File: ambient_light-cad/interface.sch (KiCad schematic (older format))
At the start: 0 parts

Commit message: [Updated] move interface page and global label
interface 페이지에 들어가는 부품 이동 및 페이지 간 라벨링을 위해 Global label로 변경
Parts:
- added C?: 4.7μF, symbol Device:CP1_Small
- added C? (x4): 220μF, symbol Device:CP1_Small
- added J?: USB_C_Receptacle_USB2.0, symbol Connector:USB_C_Receptacle_USB2.0
- added J?: LED_Strip_conn_1, symbol Connector:Conn_01x03_Female
- added J?: LED_Strip_conn_2, symbol Connector:Conn_01x03_Female
- added J?: ICSP, symbol Connector_Generic:Conn_02x03_Odd_Even
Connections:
- net labels added: +5V, D+, D-, D6, D7, GND, MISO, MOSI, Reset, SCK, VBUS, VCC
- wire segments 0 -> 42
- no-connect marks 0 -> 4

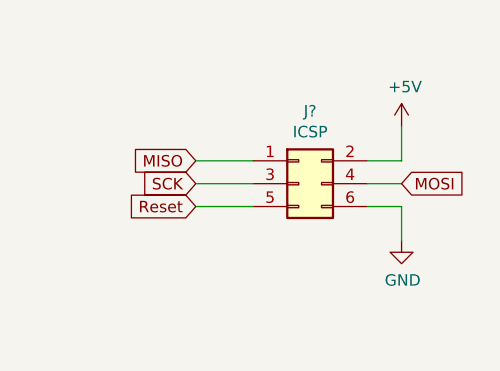
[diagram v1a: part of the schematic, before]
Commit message: [Modified] +5V to VCC /interface
전에 USBVCC와 레귤레이터 5V 분리를 위해서 섞인 VCC와 +5V를 단일화 시킴
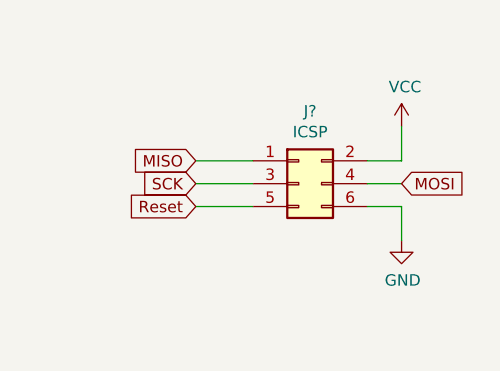
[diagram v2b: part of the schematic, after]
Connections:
- net labels removed: +5V
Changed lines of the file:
@@
 	7750 1750 7750 1900
-$Comp
-L power:+5V #PWR?
-U 1 1 5FDA9512
-P 7750 1400
-AR Path="/5FDA9512" Ref="#PWR?"  Part="1"
-AR Path="/5FD145BE/5FDA9512" Ref="#PWR?"  Part="1"
-AR Path="/5FD145BE/5FD7B477/5FDA9512" Ref="#PWR?"  Part="1"
-F 0 "#PWR?" H 7750 1250 50  0001 C CNN
-F 1 "+5V" H 7765 1573 50  0000 C CNN
-F 2 "" H 7750 1400 50  0001 C CNN
-F 3 "" H 7750 1400 50  0001 C CNN
-	1    7750 1400
-	1    0    0    -1
-$EndComp
 $Comp
 L power:GND #PWR?
@@
 Text GLabel 6850 1750 0    50   Input ~ 0
 Reset
+$Comp
+L power:VCC #PWR?
+U 1 1 5FE47264
+P 7750 1400
+AR Path="/5FE47264" Ref="#PWR?"  Part="1"
+AR Path="/5FD145BE/5FE47264" Ref="#PWR?"  Part="1"
+AR Path="/5FD145BE/5FD7B477/5FE47264" Ref="#PWR?"  Part="1"
+F 0 "#PWR?" H 7750 1250 50  0001 C CNN
+F 1 "VCC" H 7765 1573 50  0000 C CNN
+F 2 "" H 7750 1400 50  0001 C CNN
+F 3 "" H 7750 1400 50  0001 C CNN
+	1    7750 1400
+	1    0    0    -1
+$EndComp
 $EndSCHEMATC

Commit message: [Modified] μF to uF
표기에 혼동 및 어려움으로 인해 간략하게 변경
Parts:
- C?: value 4.7μF -> 4.7uF
- C? (x4): value 220μF -> 220uF
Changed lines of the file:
@@
 AR Path="/5FD145BE/5FD7B477/5FD84D97" Ref="C?"  Part="1"
 F 0 "C?" H 2941 1646 50  0000 L CNN
-F 1 "4.7μF" H 2941 1555 50  0000 L CNN
+F 1 "4.7uF" H 2941 1555 50  0000 L CNN
 F 2 "" H 2850 1600 50  0001 C CNN
 F 3 "~" H 2850 1600 50  0001 C CNN
@@
 AR Path="/5FD145BE/5FD7B477/5FD987D1" Ref="C?"  Part="1"
 F 0 "C?" H 4491 1596 50  0000 L CNN
-F 1 "220μF" H 4491 1505 50  0000 L CNN
+F 1 "220uF" H 4491 1505 50  0000 L CNN
 F 2 "" H 4400 1550 50  0001 C CNN
 F 3 "~" H 4400 1550 50  0001 C CNN
@@
 	4200 1750 4200 1650
 $Comp
-L Device:CP1_Small C?
-U 1 1 5FD987E5
-P 4200 1550
-AR Path="/5FD987E5" Ref="C?"  Part="1"
-AR Path="/5FD145BE/5FD987E5" Ref="C?"  Part="1"
-AR Path="/5FD145BE/5FD7B477/5FD987E5" Ref="C?"  Part="1"
-F 0 "C?" H 4291 1596 50  0000 L CNN
-F 1 "220μF" H 4291 1505 50  0000 L CNN
-F 2 "" H 4200 1550 50  0001 C CNN
-F 3 "~" H 4200 1550 50  0001 C CNN
-	1    4200 1550
-	-1   0    0    -1
-$EndComp
-$Comp
 L power:VCC #PWR?
 U 1 1 5FD987EB
@@
 AR Path="/5FD145BE/5FD7B477/5FD987F9" Ref="C?"  Part="1"
 F 0 "C?" H 4491 2696 50  0000 L CNN
-F 1 "220μF" H 4491 2605 50  0000 L CNN
+F 1 "220uF" H 4491 2605 50  0000 L CNN
 F 2 "" H 4400 2650 50  0001 C CNN
 F 3 "~" H 4400 2650 50  0001 C CNN
@@
 AR Path="/5FD145BE/5FD7B477/5FD9880D" Ref="C?"  Part="1"
 F 0 "C?" H 4291 2696 50  0000 L CNN
-F 1 "220μF" H 4291 2605 50  0000 L CNN
+F 1 "220uF" H 4291 2605 50  0000 L CNN
 F 2 "" H 4200 2650 50  0001 C CNN
 F 3 "~" H 4200 2650 50  0001 C CNN
@@
 	1    0    0    -1
 $EndComp
+$Comp
+L Device:CP1_Small C?
+U 1 1 5FD987E5
+P 4200 1550
+AR Path="/5FD987E5" Ref="C?"  Part="1"
+AR Path="/5FD145BE/5FD987E5" Ref="C?"  Part="1"
+AR Path="/5FD145BE/5FD7B477/5FD987E5" Ref="C?"  Part="1"
+F 0 "C?" H 4291 1596 50  0000 L CNN
+F 1 "220uF" H 4291 1505 50  0000 L CNN
+F 2 "" H 4200 1550 50  0001 C CNN
+F 3 "~" H 4200 1550 50  0001 C CNN
+	1    4200 1550
+	-1   0    0    -1
+$EndComp
 $EndSCHEMATC

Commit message: [Modified] moved RST sel SW, BT
mcu file to interface file
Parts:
- added C?: 100nF, symbol Device:C_Small
- added R? (x2): 1k, symbol Device:R_Small_US
- added SW?: SW_SPDT, symbol Switch:SW_SPDT
- added SW?: SW_Reset, symbol Switch:SW_Push
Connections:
- net labels added: D5, RST_MOS
- wire segments 42 -> 57
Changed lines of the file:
@@
 	-1   0    0    -1
 $EndComp
+Text GLabel 7900 2500 2    50   Input ~ 0
+Reset
+Text GLabel 7050 2600 0    50   Input ~ 0
+RST_MOS
+$Comp
+L Switch:SW_SPDT SW?
+U 1 1 5FED71D9
+P 7400 2600
+AR Path="/5FD145BE/5FED71D9" Ref="SW?"  Part="1"
+AR Path="/5FD145BE/5FD7B477/5FED71D9" Ref="SW?"  Part="1"
+F 0 "SW?" H 7400 2885 50  0000 C CNN
+F 1 "SW_SPDT" H 7400 2794 50  0000 C CNN
+F 2 "" H 7400 2600 50  0001 C CNN
+F 3 "~" H 7400 2600 50  0001 C CNN
+	1    7400 2600
+	1    0    0    -1
+$EndComp
+Wire Wire Line
+	7050 2600 7200 2600
+Text GLabel 7900 2700 2    50   Input ~ 0
+D5
+Wire Wire Line
+	7600 2700 7750 2700
+$Comp
+L Device:R_Small_US R?
+U 1 1 5FED71E2
+P 7750 2900
+AR Path="/5FED71E2" Ref="R?"  Part="1"
+AR Path="/5FD145BE/5FED71E2" Ref="R?"  Part="1"
+AR Path="/5FD145BE/5FD7B477/5FED71E2" Ref="R?"  Part="1"
+F 0 "R?" H 7809 2946 50  0000 L CNN
+F 1 "1k" H 7809 2855 50  0000 L CNN
+F 2 "" H 7750 2900 50  0001 C CNN
+F 3 "~" H 7750 2900 50  0001 C CNN
+	1    7750 2900
+	1    0    0    -1
+$EndComp
+Wire Wire Line
+	7750 2800 7750 2700
+Connection ~ 7750 2700
+Wire Wire Line
+	7750 2700 7900 2700
+$Comp
+L power:GND #PWR?
+U 1 1 5FED71EB
+P 7750 3100
+AR Path="/5FED71EB" Ref="#PWR?"  Part="1"
+AR Path="/5FD145BE/5FED71EB" Ref="#PWR?"  Part="1"
+AR Path="/5FD145BE/5FD7B477/5FED71EB" Ref="#PWR?"  Part="1"
+F 0 "#PWR?" H 7750 2850 50  0001 C CNN
+F 1 "GND" H 7755 2927 50  0000 C CNN
+F 2 "" H 7750 3100 50  0001 C CNN
+F 3 "" H 7750 3100 50  0001 C CNN
+	1    7750 3100
+	1    0    0    -1
+$EndComp
+Wire Wire Line
+	7750 3100 7750 3000
+Wire Wire Line
+	7600 2500 7900 2500
+$Comp
+L Device:R_Small_US R?
+U 1 1 5FEDED8A
+P 9200 1550
+AR Path="/5FEDED8A" Ref="R?"  Part="1"
+AR Path="/5FD145BE/5FEDED8A" Ref="R?"  Part="1"
+F 0 "R?" H 9259 1596 50  0000 L CNN
+F 1 "1k" H 9259 1505 50  0000 L CNN
+F 2 "" H 9200 1550 50  0001 C CNN
+F 3 "~" H 9200 1550 50  0001 C CNN
+	1    9200 1550
+	1    0    0    -1
+$EndComp
+$Comp
+L Switch:SW_Push SW?
+U 1 1 5FEDED90
+P 9200 2150
+AR Path="/5FEDED90" Ref="SW?"  Part="1"
+AR Path="/5FD145BE/5FEDED90" Ref="SW?"  Part="1"
+F 0 "SW?" V 9150 2400 50  0000 C CNN
+F 1 "SW_Reset" V 9250 2500 50  0000 C CNN
+F 2 "" H 9200 2350 50  0001 C CNN
+F 3 "~" H 9200 2350 50  0001 C CNN
+	1    9200 2150
+	0    1    1    0
+$EndComp
+Text GLabel 9450 1800 2    50   Input ~ 0
+Reset
+$Comp
+L power:VCC #PWR?
+U 1 1 5FEDED97
+P 9200 1350
+AR Path="/5FEDED97" Ref="#PWR?"  Part="1"
+AR Path="/5FD145BE/5FEDED97" Ref="#PWR?"  Part="1"
+F 0 "#PWR?" H 9200 1200 50  0001 C CNN
+F 1 "VCC" H 9215 1523 50  0000 C CNN
+F 2 "" H 9200 1350 50  0001 C CNN
+F 3 "" H 9200 1350 50  0001 C CNN
+	1    9200 1350
+	1    0    0    -1
+$EndComp
+$Comp
+L Device:C_Small C?
+U 1 1 5FEDED9D
+P 9000 2150
+F 0 "C?" H 9092 2196 50  0000 L CNN
+F 1 "100nF" H 9092 2105 50  0000 L CNN
+F 2 "" H 9000 2150 50  0001 C CNN
+F 3 "~" H 9000 2150 50  0001 C CNN
+	1    9000 2150
+	-1   0    0    -1
+$EndComp
+Wire Wire Line
+	9000 2050 9000 1950
+Wire Wire Line
+	9000 2250 9000 2350
+Connection ~ 9200 1950
+Wire Wire Line
+	9200 2350 9200 2500
+Connection ~ 9200 2350
+Wire Wire Line
+	9000 1950 9200 1950
+$Comp
+L power:GND #PWR?
+U 1 1 5FEDEDA9
+P 9200 2500
+AR Path="/5FEDEDA9" Ref="#PWR?"  Part="1"
+AR Path="/5FD145BE/5FEDEDA9" Ref="#PWR?"  Part="1"
+F 0 "#PWR?" H 9200 2250 50  0001 C CNN
+F 1 "GND" H 9205 2327 50  0000 C CNN
+F 2 "" H 9200 2500 50  0001 C CNN
+F 3 "" H 9200 2500 50  0001 C CNN
+	1    9200 2500
+	1    0    0    -1
+$EndComp
+Wire Wire Line
+	9000 2350 9200 2350
+Wire Wire Line
+	9200 1350 9200 1450
+Wire Wire Line
+	9200 1650 9200 1800
+Wire Wire Line
+	9450 1800 9200 1800
+Connection ~ 9200 1800
+Wire Wire Line
+	9200 1800 9200 1950
 $EndSCHEMATC

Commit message: [Updated] Symbol field for PCB layout
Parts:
- C? (x2): footprint (none) -> Capacitor_SMD:C_0603_1608Metric_Pad1.08x0.95mm_HandSolder
- C? (x4): footprint (none) -> Capacitor_Tantalum_SMD:CP_EIA-7343-31_Kemet-D_Pad2.25x2.55mm_HandSolder
- J?: footprint (none) -> Connector_USB:USB_C_Receptacle_Amphenol_12401610E4-2A
- J?: footprint (none) -> Connector_Molex:Molex_Micro-Fit_3.0_43045-1815_2x09_P3.00mm_Vertical
- J?: footprint (none) -> Connector_Molex:Molex_CLIK-Mate_505405-0570_1x05-1MP_P1.50mm_Vertical
- J?: footprint (none) -> Connector_PinSocket_2.54mm:PinSocket_2x03_P2.54mm_Vertical
- R? (x2): footprint (none) -> Resistor_SMD:R_0603_1608Metric_Pad0.98x0.95mm_HandSolder
- SW?: footprint (none) -> Button_Switch_SMD:SW_SPDT_PCM12
- SW?: footprint (none) -> Button_Switch_SMD:SW_SPST_CK_RS282G05A3
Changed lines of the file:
@@
 F 0 "C?" H 2941 1646 50  0000 L CNN
 F 1 "4.7uF" H 2941 1555 50  0000 L CNN
-F 2 "" H 2850 1600 50  0001 C CNN
+F 2 "Capacitor_SMD:C_0603_1608Metric_Pad1.08x0.95mm_HandSolder" H 2850 1600 50  0001 C CNN
 F 3 "~" H 2850 1600 50  0001 C CNN
 	1    2850 1600
@@
 F 0 "J?" H 1757 2817 50  0000 C CNN
 F 1 "USB_C_Receptacle_USB2.0" H 1757 2726 50  0000 C CNN
-F 2 "" H 1800 1950 50  0001 C CNN
+F 2 "Connector_USB:USB_C_Receptacle_Amphenol_12401610E4-2A" H 1800 1950 50  0001 C CNN
 F 3 "https://www.usb.org/sites/default/files/documents/usb_type-c.zip" H 1800 1950 50  0001 C CNN
 	1    1650 1950
@@
 F 0 "J?" H 5378 1576 50  0000 L CNN
 F 1 "LED_Strip_conn_1" H 5378 1485 50  0000 L CNN
-F 2 "" H 5350 1550 50  0001 C CNN
+F 2 "Connector_Molex:Molex_Micro-Fit_3.0_43045-1815_2x09_P3.00mm_Vertical" H 5350 1550 50  0001 C CNN
 F 3 "~" H 5350 1550 50  0001 C CNN
 	1    5350 1550
@@
 F 0 "J?" H 5378 2676 50  0000 L CNN
 F 1 "LED_Strip_conn_2" H 5378 2585 50  0000 L CNN
-F 2 "" H 5350 2650 50  0001 C CNN
+F 2 "Connector_Molex:Molex_CLIK-Mate_505405-0570_1x05-1MP_P1.50mm_Vertical" H 5350 2650 50  0001 C CNN
 F 3 "~" H 5350 2650 50  0001 C CNN
 	1    5350 2650
@@
 F 0 "C?" H 4491 1596 50  0000 L CNN
 F 1 "220uF" H 4491 1505 50  0000 L CNN
-F 2 "" H 4400 1550 50  0001 C CNN
+F 2 "Capacitor_Tantalum_SMD:CP_EIA-7343-31_Kemet-D_Pad2.25x2.55mm_HandSolder" H 4400 1550 50  0001 C CNN
 F 3 "~" H 4400 1550 50  0001 C CNN
 	1    4400 1550
@@
 F 0 "C?" H 4491 2696 50  0000 L CNN
 F 1 "220uF" H 4491 2605 50  0000 L CNN
-F 2 "" H 4400 2650 50  0001 C CNN
+F 2 "Capacitor_Tantalum_SMD:CP_EIA-7343-31_Kemet-D_Pad2.25x2.55mm_HandSolder" H 4400 2650 50  0001 C CNN
 F 3 "~" H 4400 2650 50  0001 C CNN
 	1    4400 2650
@@
 F 0 "C?" H 4291 2696 50  0000 L CNN
 F 1 "220uF" H 4291 2605 50  0000 L CNN
-F 2 "" H 4200 2650 50  0001 C CNN
+F 2 "Capacitor_Tantalum_SMD:CP_EIA-7343-31_Kemet-D_Pad2.25x2.55mm_HandSolder" H 4200 2650 50  0001 C CNN
 F 3 "~" H 4200 2650 50  0001 C CNN
 	1    4200 2650
@@
 F 0 "J?" H 7350 1967 50  0000 C CNN
 F 1 "ICSP" H 7350 1876 50  0000 C CNN
-F 2 "" H 7300 1650 50  0001 C CNN
+F 2 "Connector_PinSocket_2.54mm:PinSocket_2x03_P2.54mm_Vertical" H 7300 1650 50  0001 C CNN
 F 3 "~" H 7300 1650 50  0001 C CNN
 	1    7300 1650
@@
 F 0 "C?" H 4291 1596 50  0000 L CNN
 F 1 "220uF" H 4291 1505 50  0000 L CNN
-F 2 "" H 4200 1550 50  0001 C CNN
+F 2 "Capacitor_Tantalum_SMD:CP_EIA-7343-31_Kemet-D_Pad2.25x2.55mm_HandSolder" H 4200 1550 50  0001 C CNN
 F 3 "~" H 4200 1550 50  0001 C CNN
 	1    4200 1550
@@
 F 0 "SW?" H 7400 2885 50  0000 C CNN
 F 1 "SW_SPDT" H 7400 2794 50  0000 C CNN
-F 2 "" H 7400 2600 50  0001 C CNN
+F 2 "Button_Switch_SMD:SW_SPDT_PCM12" H 7400 2600 50  0001 C CNN
 F 3 "~" H 7400 2600 50  0001 C CNN
 	1    7400 2600
@@
 F 0 "R?" H 7809 2946 50  0000 L CNN
 F 1 "1k" H 7809 2855 50  0000 L CNN
-F 2 "" H 7750 2900 50  0001 C CNN
+F 2 "Resistor_SMD:R_0603_1608Metric_Pad0.98x0.95mm_HandSolder" H 7750 2900 50  0001 C CNN
 F 3 "~" H 7750 2900 50  0001 C CNN
 	1    7750 2900
@@
 AR Path="/5FEDED8A" Ref="R?"  Part="1"
 AR Path="/5FD145BE/5FEDED8A" Ref="R?"  Part="1"
+AR Path="/5FD145BE/5FD7B477/5FEDED8A" Ref="R?"  Part="1"
 F 0 "R?" H 9259 1596 50  0000 L CNN
 F 1 "1k" H 9259 1505 50  0000 L CNN
-F 2 "" H 9200 1550 50  0001 C CNN
+F 2 "Resistor_SMD:R_0603_1608Metric_Pad0.98x0.95mm_HandSolder" H 9200 1550 50  0001 C CNN
 F 3 "~" H 9200 1550 50  0001 C CNN
 	1    9200 1550
@@
 AR Path="/5FEDED90" Ref="SW?"  Part="1"
 AR Path="/5FD145BE/5FEDED90" Ref="SW?"  Part="1"
+AR Path="/5FD145BE/5FD7B477/5FEDED90" Ref="SW?"  Part="1"
 F 0 "SW?" V 9150 2400 50  0000 C CNN
 F 1 "SW_Reset" V 9250 2500 50  0000 C CNN
-F 2 "" H 9200 2350 50  0001 C CNN
+F 2 "Button_Switch_SMD:SW_SPST_CK_RS282G05A3" H 9200 2350 50  0001 C CNN
 F 3 "~" H 9200 2350 50  0001 C CNN
 	1    9200 2150
@@
 AR Path="/5FEDED97" Ref="#PWR?"  Part="1"
 AR Path="/5FD145BE/5FEDED97" Ref="#PWR?"  Part="1"
+AR Path="/5FD145BE/5FD7B477/5FEDED97" Ref="#PWR?"  Part="1"
 F 0 "#PWR?" H 9200 1200 50  0001 C CNN
 F 1 "VCC" H 9215 1523 50  0000 C CNN
@@
 F 0 "C?" H 9092 2196 50  0000 L CNN
 F 1 "100nF" H 9092 2105 50  0000 L CNN
-F 2 "" H 9000 2150 50  0001 C CNN
+F 2 "Capacitor_SMD:C_0603_1608Metric_Pad1.08x0.95mm_HandSolder" H 9000 2150 50  0001 C CNN
 F 3 "~" H 9000 2150 50  0001 C CNN
 	1    9000 2150
@@
 AR Path="/5FEDEDA9" Ref="#PWR?"  Part="1"
 AR Path="/5FD145BE/5FEDEDA9" Ref="#PWR?"  Part="1"
+AR Path="/5FD145BE/5FD7B477/5FEDEDA9" Ref="#PWR?"  Part="1"
 F 0 "#PWR?" H 9200 2250 50  0001 C CNN
 F 1 "GND" H 9205 2327 50  0000 C CNN

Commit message: [Updated] Net list
set connector footprint
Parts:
- J?: footprint Connector_Molex:Molex_Micro-Fit_3.0_43045-1815_2x09_P3.00mm_Vertical -> ambient_light-cad:NW-HA2.5-3AW_Horizontal
- J?: footprint Connector_Molex:Molex_CLIK-Mate_505405-0570_1x05-1MP_P1.50mm_Vertical -> ambient_light-cad:NW-HA2.5-3AW_Horizontal
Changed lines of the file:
@@
 F 0 "J?" H 5378 1576 50  0000 L CNN
 F 1 "LED_Strip_conn_1" H 5378 1485 50  0000 L CNN
-F 2 "Connector_Molex:Molex_Micro-Fit_3.0_43045-1815_2x09_P3.00mm_Vertical" H 5350 1550 50  0001 C CNN
+F 2 "ambient_light-cad:NW-HA2.5-3AW_Horizontal" H 5350 1550 50  0001 C CNN
 F 3 "~" H 5350 1550 50  0001 C CNN
 	1    5350 1550
@@
 F 0 "J?" H 5378 2676 50  0000 L CNN
 F 1 "LED_Strip_conn_2" H 5378 2585 50  0000 L CNN
-F 2 "Connector_Molex:Molex_CLIK-Mate_505405-0570_1x05-1MP_P1.50mm_Vertical" H 5350 2650 50  0001 C CNN
+F 2 "ambient_light-cad:NW-HA2.5-3AW_Horizontal" H 5350 2650 50  0001 C CNN
 F 3 "~" H 5350 2650 50  0001 C CNN
 	1    5350 2650

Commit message: ICSP PinSocket to PinHeader
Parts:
- J?: symbol Connector:USB_C_Receptacle_USB2.0 -> ambient_light-cad-rescue:USB_C_Receptacle_USB2.0-Connector
- J?: footprint Connector_PinSocket_2.54mm:PinSocket_2x03_P2.54mm_Vertical -> Connector_PinHeader_2.54mm:PinHeader_2x03_P2.54mm_Vertical
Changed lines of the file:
@@
 $EndComp
 $Comp
-L Connector:USB_C_Receptacle_USB2.0 J?
+L ambient_light-cad-rescue:USB_C_Receptacle_USB2.0-Connector J?
 U 1 1 5FD84D9D
 P 1650 1950
 AR Path="/5FD145BE/5FD84D9D" Ref="J?"  Part="1"
 AR Path="/5FD145BE/5FD7B477/5FD84D9D" Ref="J?"  Part="1"
+AR Path="/5FD84D9D" Ref="J?"  Part="1"
 F 0 "J?" H 1757 2817 50  0000 C CNN
 F 1 "USB_C_Receptacle_USB2.0" H 1757 2726 50  0000 C CNN
@@
 F 0 "J?" H 7350 1967 50  0000 C CNN
 F 1 "ICSP" H 7350 1876 50  0000 C CNN
-F 2 "Connector_PinSocket_2.54mm:PinSocket_2x03_P2.54mm_Vertical" H 7300 1650 50  0001 C CNN
+F 2 "Connector_PinHeader_2.54mm:PinHeader_2x03_P2.54mm_Vertical" H 7300 1650 50  0001 C CNN
 F 3 "~" H 7300 1650 50  0001 C CNN
 	1    7300 1650
